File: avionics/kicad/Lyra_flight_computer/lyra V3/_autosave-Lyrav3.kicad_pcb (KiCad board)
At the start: 2 copper layers, 25 x 80 mm, 88 parts, among them J1 USB_B_Micro, J11 Conn_02x03_Odd_Even, J12 Conn_02x03_Odd_Even, J13 Conn_02x03_Odd_Even, J14 Conn_01x04, J15 Conn_01x04, J16 Conn_01x03, J17 MEM2067-02-180-00-A, J18 1862372, J2 1862372, J6 Conn_02x03_Odd_Even, Q1 AO3401A, Q2 BSS138, Q3 BSS138, SW1 SW_Push_DPDT, U1 AZ1117-3.3, U2 AZ1117-5.0, U3 LIS3MDL, U4 BMP390L, U5 W25Q128JVS, U6 RP2040, U7 BMI088, X1 ECS-2520MV-xxx-xx

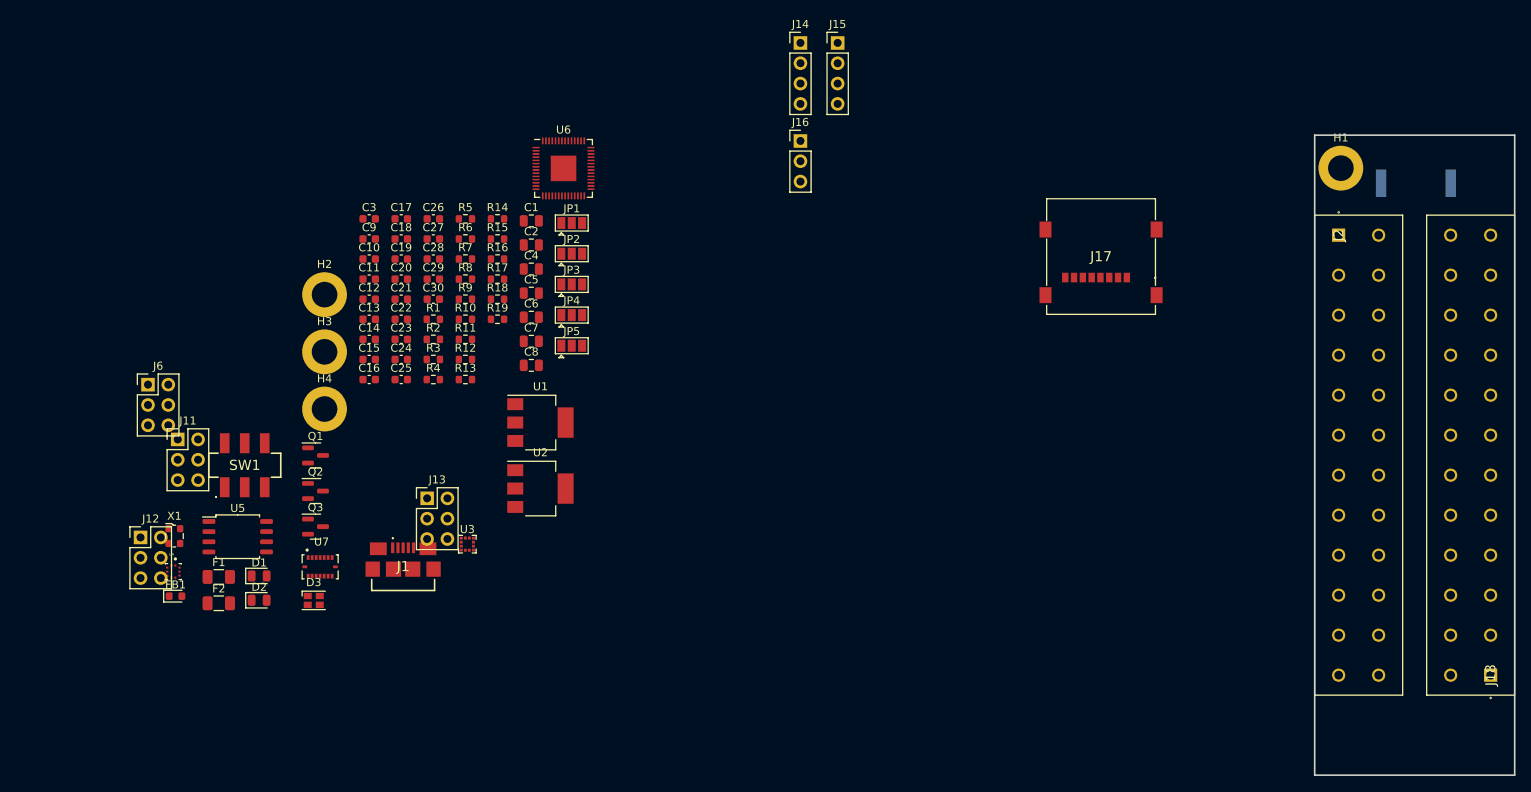
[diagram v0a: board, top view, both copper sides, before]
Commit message: lyra v3 work
got most of the sensors and other stuff picked out
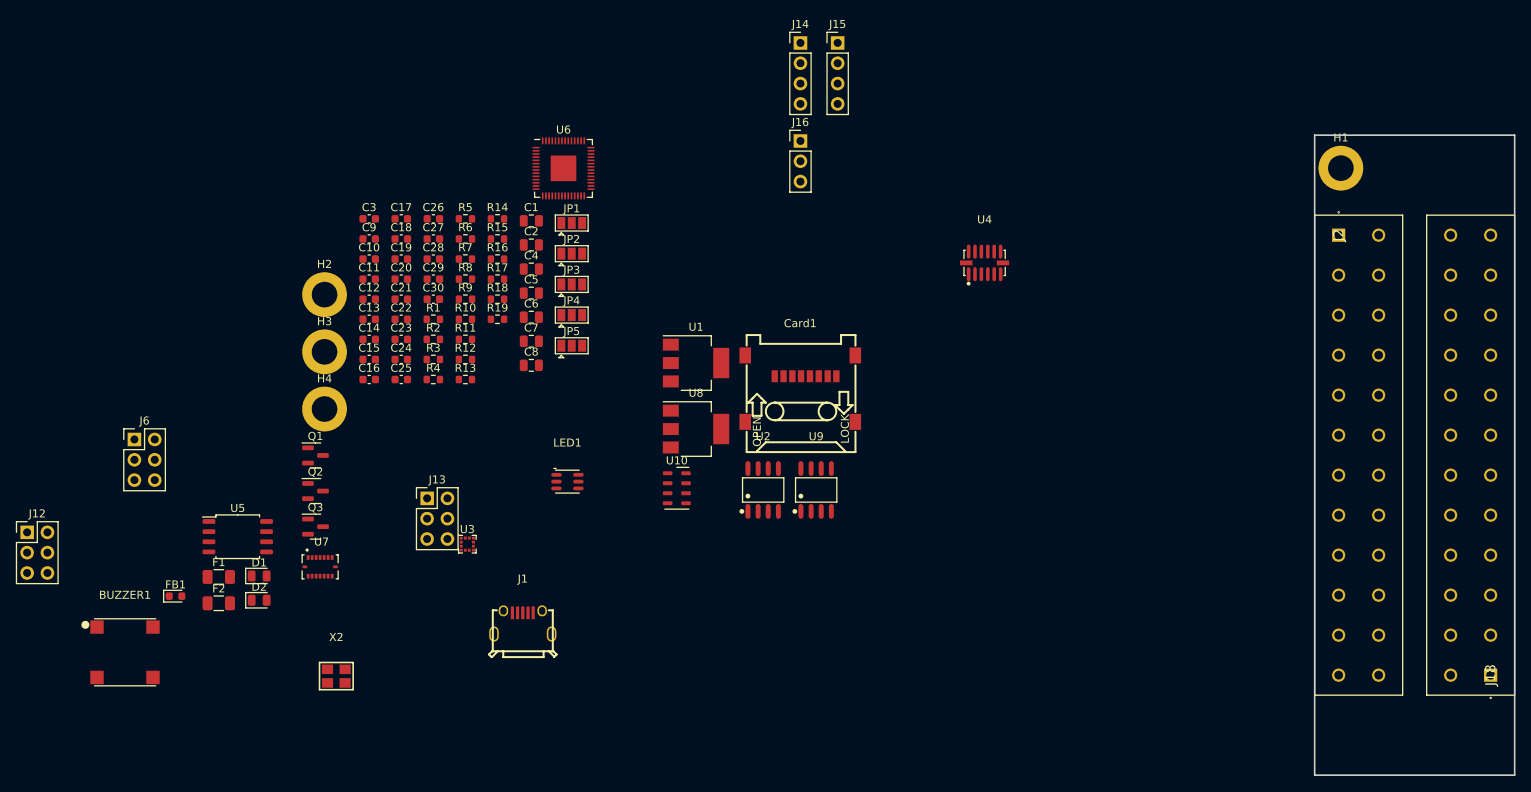
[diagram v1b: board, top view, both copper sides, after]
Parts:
- removed D3: CLV1L-FKB, LED_SMD:LED_Cree-PLCC4_2x2mm_CW
- removed J11: Conn_02x03_Odd_Even, Connector_PinHeader_2.54mm:PinHeader_2x03_P2.54mm_Vertical
- removed J17: MEM2067-02-180-00-A, SamacSys_Parts:MEM20670218000A
- removed LS1: PKMCS0909E4000-R1, SamacSys_Parts:PKMCS0909E4000R1
- removed SW1: SW_Push_DPDT, SamacSys_Parts:JS202011SCQN
- removed X1: ECS-2520MV-xxx-xx, Oscillator:Oscillator_SMD_ECS_2520MV-xxx-xx-4Pin_2.5x2.0mm
- added BUZZER1: MLT-7525, easyeda2kicad:BUZ-SMD_4P-L7.5-W7.5-P7.59-TL, F.Cu at (34.9, 103.7)
- added Card1: TF-002-H18, easyeda2kicad:SIM-SMD_TF-002-H18, F.Cu at (119.3, 70.7)
- added LED1: FM-Z2727RGBA-SH, easyeda2kicad:LED-SMD_6P-L2.7-W2.8-TL, F.Cu at (90.2, 82.3)
- added U10: MPL3115A2, Package_LGA:NXP_LGA-8_3x5mm_P1.25mm_H1.1mm, F.Cu at (103.9, 83.2)
- added U8: AMS1117-3.3, Package_TO_SOT_SMD:SOT-223-3_TabPin2, F.Cu at (106.3, 75.8)
- added U9: HXY9926S, easyeda2kicad:SOP-8_L4.9-W3.9-P1.27-LS6.0-BL, F.Cu at (121.3, 83.4)
- added X2: S3D12.288000B20F30T, easyeda2kicad:OSC-SMD_4P-L3.2-W2.5-BL_SIT8008BI, F.Cu at (61.3, 106.6)
- J1: footprint SamacSys_Parts:101181920001LF -> easyeda2kicad:MICRO-USB-SMD_U254-051T-4BHJ25-F2S
- U1: value AZ1117-3.3 -> AMS1117-5.0
- U2: value AZ1117-5.0 -> HXY9926S; footprint Package_TO_SOT_SMD:SOT-223-3_TabPin2 -> easyeda2kicad:SOP-8_L4.9-W3.9-P1.27-LS6.0-BL
- U4: value BMP390L -> ADXL375BCCZ-RL7; footprint SnapEDA Library:XDCR_BMP390L -> easyeda2kicad:LGA-14_L5.0-W3.0-P0.80-BL
- moved U4 108.5 mm to (142.3, 55.0)
- moved U2 27.8 mm to (114.7, 83.4)
- moved U1 20.8 mm to (106.3, 67.5)
- moved J1 16.4 mm to (84.6, 99.9)
- moved J12 14.2 mm to (22.7, 88.7)
- moved J6 7.06 mm to (36.1, 77.1)
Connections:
- U1 pad 2: +3V3 -> +5V
- U2 pad 1: GND -> unconnected-(U2-S1-Pad1)
- U2 pad 2: +5V -> unconnected-(U2-G1-Pad2)
- U2 pad 3: +12VA -> unconnected-(U2-S2-Pad3)
- U4 pad 1: +3V3 -> unconnected-(U4-VDDI/O-Pad1)
- U4 pad 10: +3V3 -> unconnected-(U4-NC-Pad10)
- U4 pad 2: /I2C1 SCL -> unconnected-(U4-GND-Pad2)
- U4 pad 3: GND -> unconnected-(U4-RESERVED-Pad3)
- U4 pad 4: /I2C1 SDA -> unconnected-(U4-GND-Pad4)
- U4 pad 5: GND -> unconnected-(U4-GND-Pad5)
- U4 pad 6: +3V3 -> unconnected-(U4-VS-Pad6)
- U4 pad 7: /BARO INT -> unconnected-(U4-~{CS}-Pad7)
- U4 pad 8: GND -> unconnected-(U4-INT1-Pad8)
- U4 pad 9: GND -> unconnected-(U4-INT2-Pad9)
- U6 pad 11: /MAG DRDY -> unconnected-(U6-GPIO8-Pad11)
- U6 pad 29: /ACCEL INT1 -> unconnected-(U6-GPIO18-Pad29)
- U6 pad 30: /ACCEL INT2 -> unconnected-(U6-GPIO19-Pad30)
- U6 pad 31: /GYRO INT3 -> unconnected-(U6-GPIO20-Pad31)
- U6 pad 32: /GYRO INT4 -> unconnected-(U6-GPIO21-Pad32)
- U6 pad 36: /MAG INT -> unconnected-(U6-GPIO24-Pad36)
- U6 pad 37: /BARO INT -> unconnected-(U6-GPIO25-Pad37)
- U6 pad 6: /BRKOUT CS -> unconnected-(U6-GPIO4-Pad6)
